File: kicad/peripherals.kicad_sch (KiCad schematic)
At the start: 22 parts, among them J4 PWR, J5 I2C1, J6 Control, J7 uSD, J8 LCD_Conn, P1 Mini-DIN-6, Q1 2N7000, U10 ESP-01-v2, U4 74HC14, U6 24LC512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

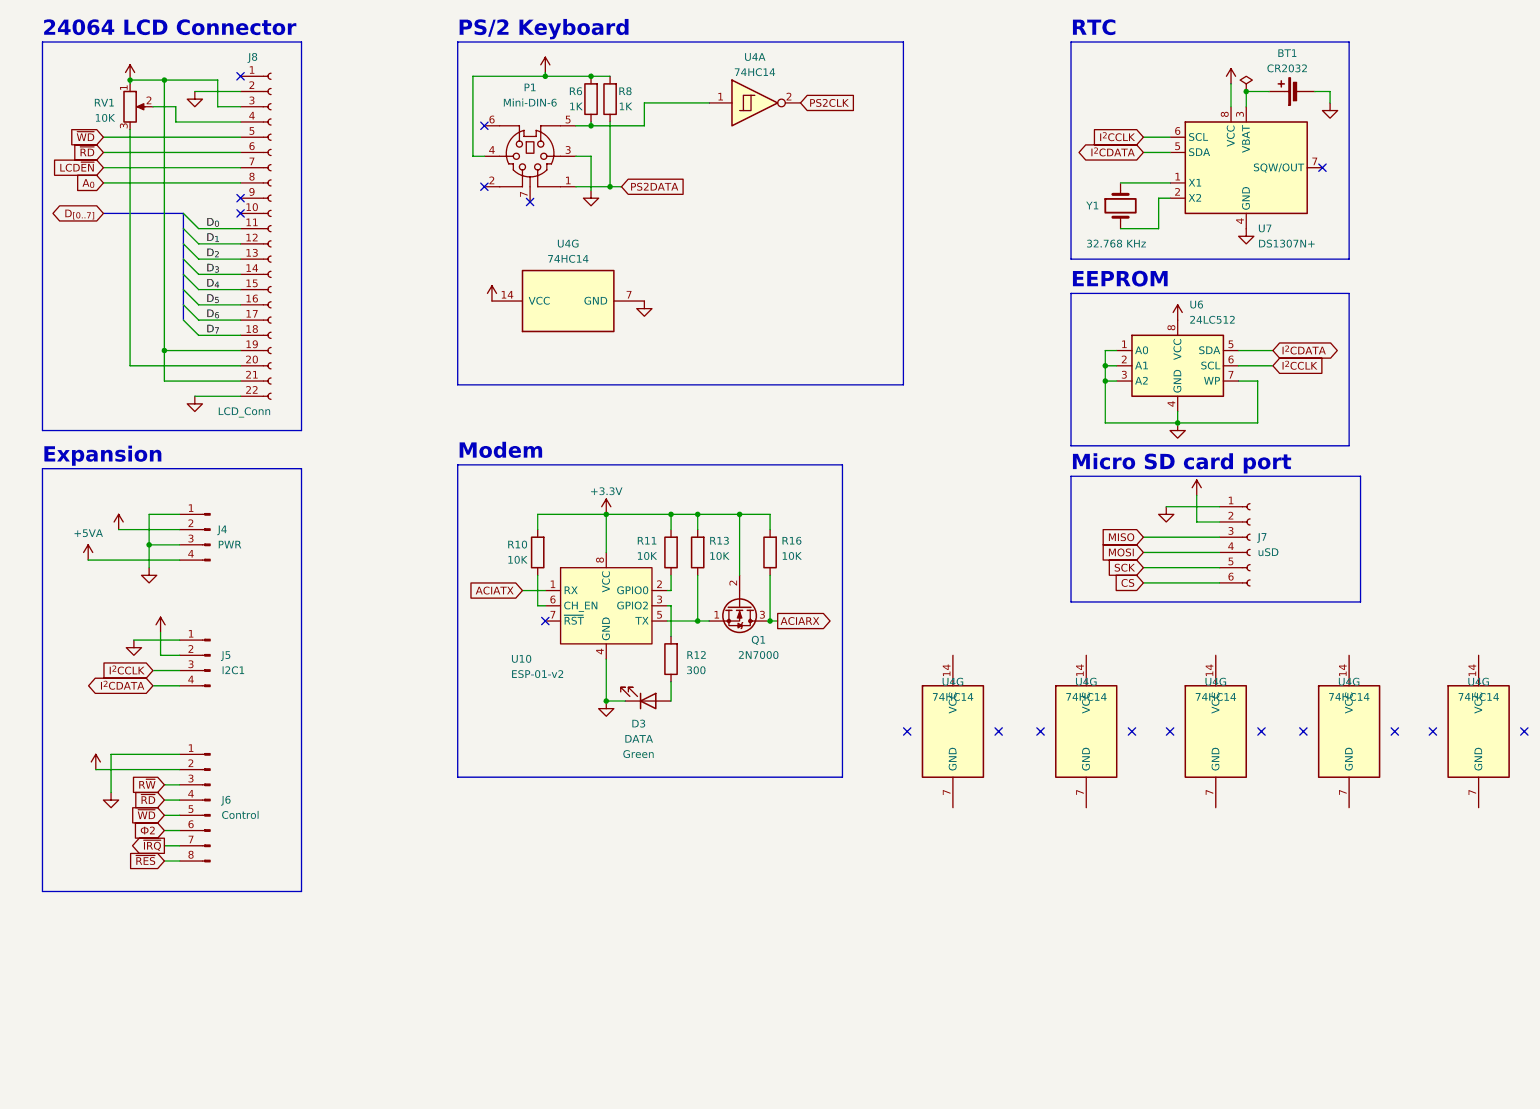
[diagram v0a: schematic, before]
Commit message: WIP: v2.0 split board
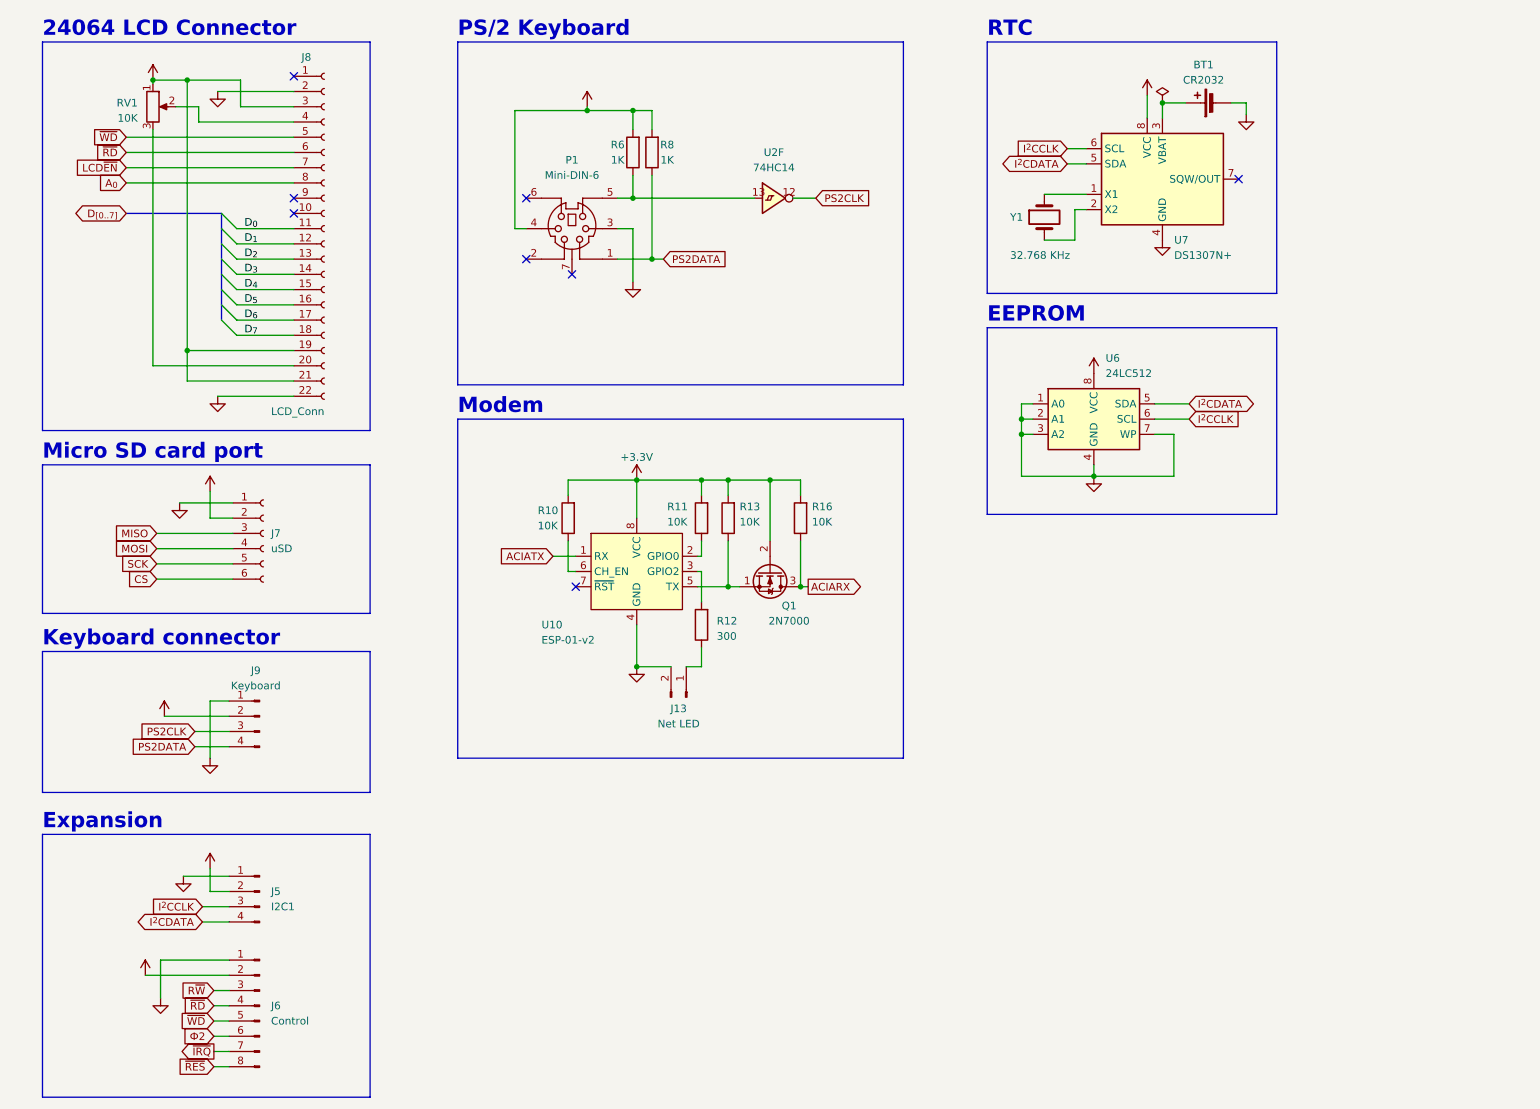
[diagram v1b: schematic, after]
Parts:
- removed D3: DATA, LED_THT:LED_D3.0mm, symbol Device:LED
- removed J4: PWR, Connector_PinHeader_2.54mm:PinHeader_2x02_P2.54mm_Vertical, symbol Connector:Conn_01x04_Pin
- removed U4 (x6): 74HC14, Package_DIP:DIP-14_W7.62mm_Socket, symbol 74xx:74HC14
- added J13: Net LED, Connector_PinHeader_2.54mm:PinHeader_1x02_P2.54mm_Vertical, symbol Connector:Conn_01x02_Pin
- added J9: Keyboard, Connector_PinHeader_2.54mm:PinHeader_1x04_P2.54mm_Vertical, symbol Connector:Conn_01x04_Pin
- added U2: 74HC14, Package_DIP:DIP-14_W7.62mm_Socket, symbol 74hc00_small:74HC14_small
- J5: footprint Connector_PinHeader_2.54mm:PinHeader_2x02_P2.54mm_Vertical -> Connector_PinHeader_2.54mm:PinHeader_1x04_P2.54mm_Vertical
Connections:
- net +5V: now also J9.2 (Pin_2)
- net GND: now also J13.2 (Pin_2), J9.1 (Pin_1)
- net PS2CLK: now also J9.3 (Pin_3), U2.12
- net PS2DATA: now also J9.4 (Pin_4)
- net at R12.1: now also J13.1 (Pin_1)
- net at P1.5, R6.1: now also U2.13
- no-connect marks 18 -> 8
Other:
- note added: "Keyboard connector"
- moved on the sheet: BT1, J5, J6, J7, J8, P1, Q1, R10, R11, R12, R13, R16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

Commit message: v2.1 updates
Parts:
- U7: footprint Package_DIP:DIP-8_W7.62mm -> Package_DIP:DIP-8_W7.62mm_Socket
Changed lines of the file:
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@@
       (effects (font (size 1.27 1.27)) (justify left))
     )
-    (property "Footprint" "Package_DIP:DIP-8_W7.62mm" (at 203.2 53.34 0)
+    (property "Footprint" "Package_DIP:DIP-8_W7.62mm_Socket" (at 203.2 53.34 0)
       (effects (font (size 1.27 1.27)) hide)
     )
